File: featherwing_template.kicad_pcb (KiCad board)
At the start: 2 copper layers, 50.8 x 22.9 mm, 3 parts

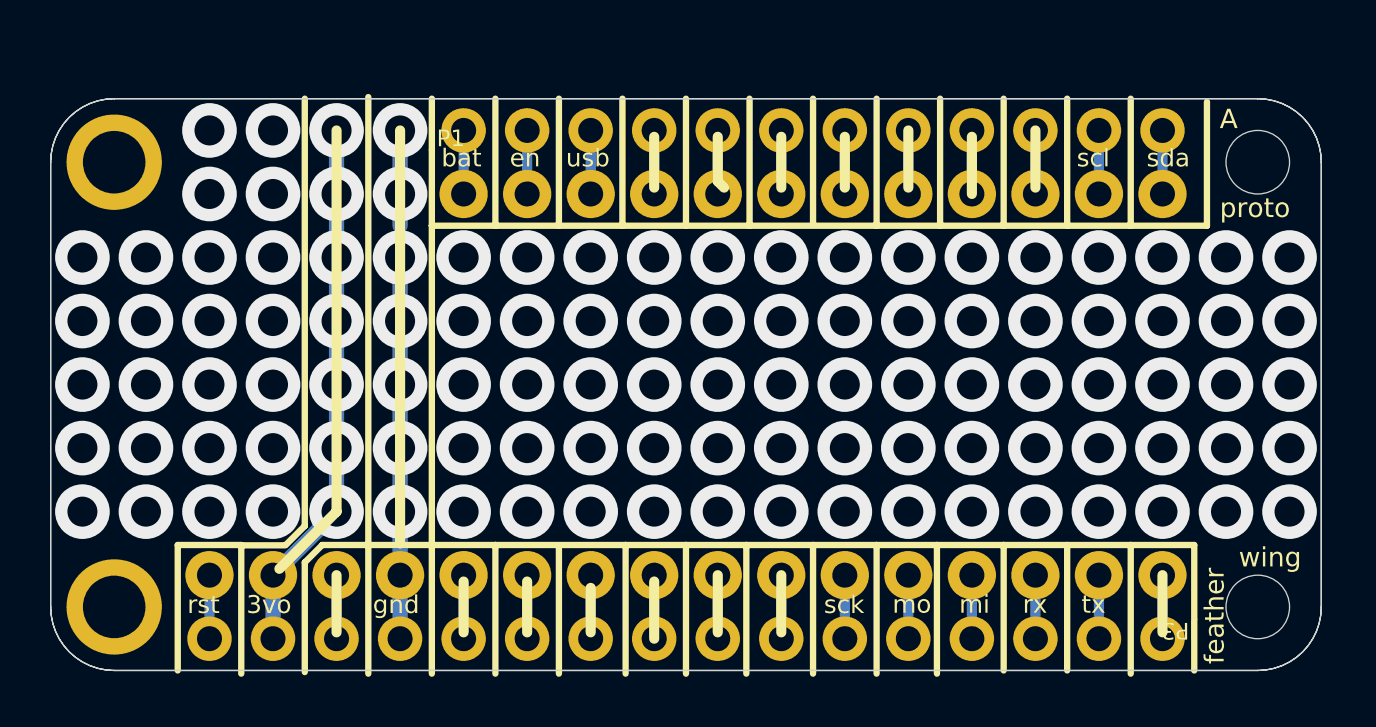
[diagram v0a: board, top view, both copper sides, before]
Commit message: Remove the silkscreen
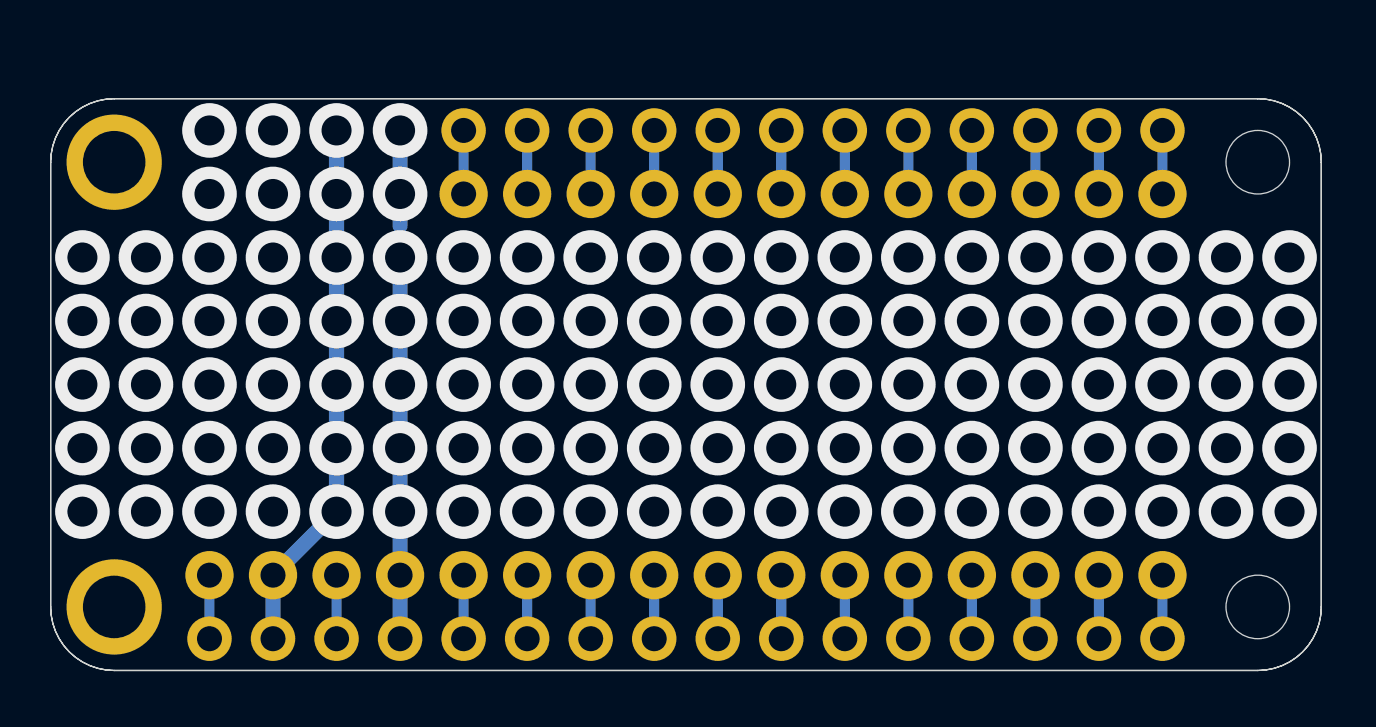
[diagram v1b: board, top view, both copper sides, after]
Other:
- board text removed: "3vo"
- board text removed: "A"
- board text removed: "bat"
- board text removed: "en"
- board text removed: "feather"
- board text removed: "gnd"
- board text removed: "mi"
- board text removed: "mo"
- board text removed: "proto"
- board text removed: "rst"
- board text removed: "rx"
- board text removed: "sck"
- board text removed: "scl"
- board text removed: "sda"
- board text removed: "tx"
- board text removed: "usb"
- board text removed: "wing"

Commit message: REmove all traces and holes (except edge ones)
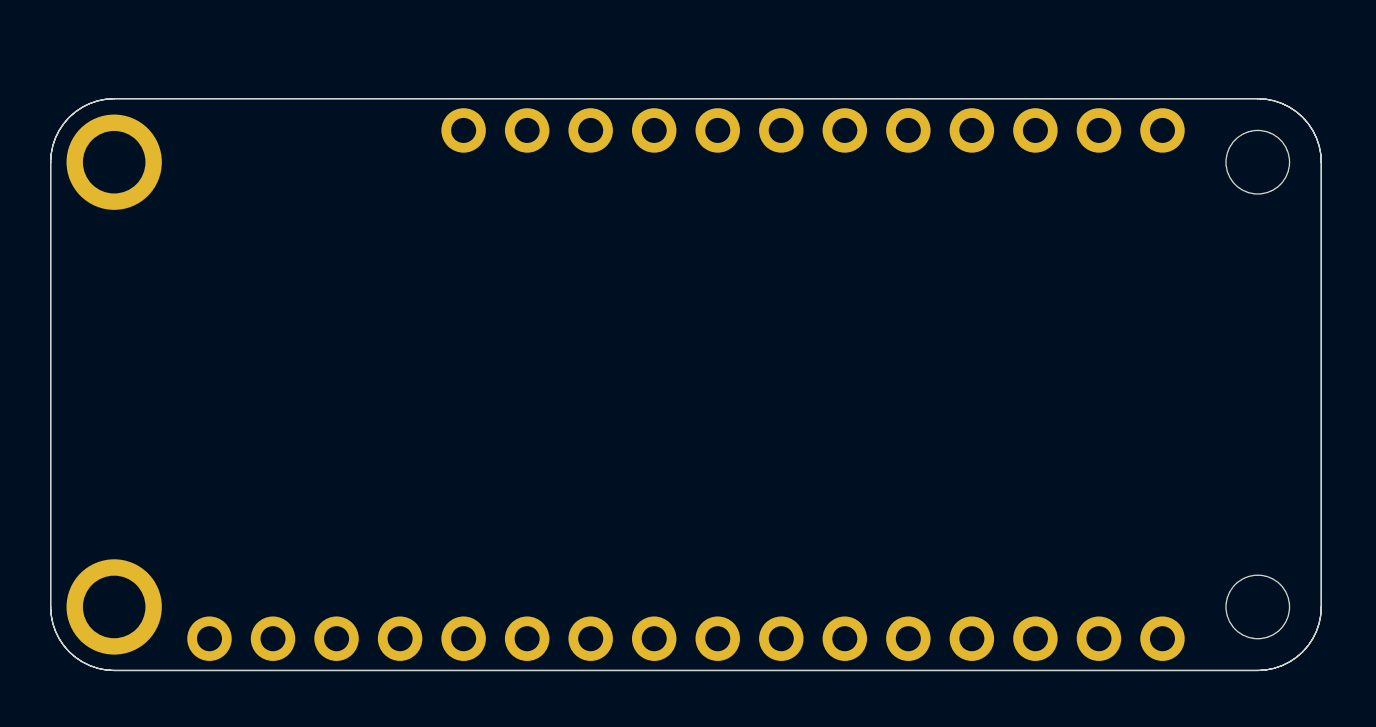
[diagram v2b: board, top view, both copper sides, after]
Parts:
- removed JP1: , featherwing_template:1X12_ROUND_76MIL
- removed JP3: , featherwing_template:1X16_ROUND_76MIL
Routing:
- net 3V: track 21.4 -> 0.00 mm, vias 7 -> 0
- net GND: track 20.3 -> 0.00 mm, vias 7 -> 0
- net VBAT: track 2.54 -> 0.00 mm
- net USB: track 2.54 -> 0.00 mm
- net N$9: track 2.54 -> 0.00 mm
- net N$8: track 2.54 -> 0.00 mm
- net N$7: track 2.54 -> 0.00 mm
- net N$6: track 2.54 -> 0.00 mm
- net N$5: track 2.54 -> 0.00 mm
- net N$4: track 2.54 -> 0.00 mm
- net N$3: track 2.54 -> 0.00 mm
- net N$25: track 2.54 -> 0.00 mm
- net N$24: track 2.54 -> 0.00 mm
- net N$23: track 2.54 -> 0.00 mm
- net N$22: track 2.54 -> 0.00 mm
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
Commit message: Add headers
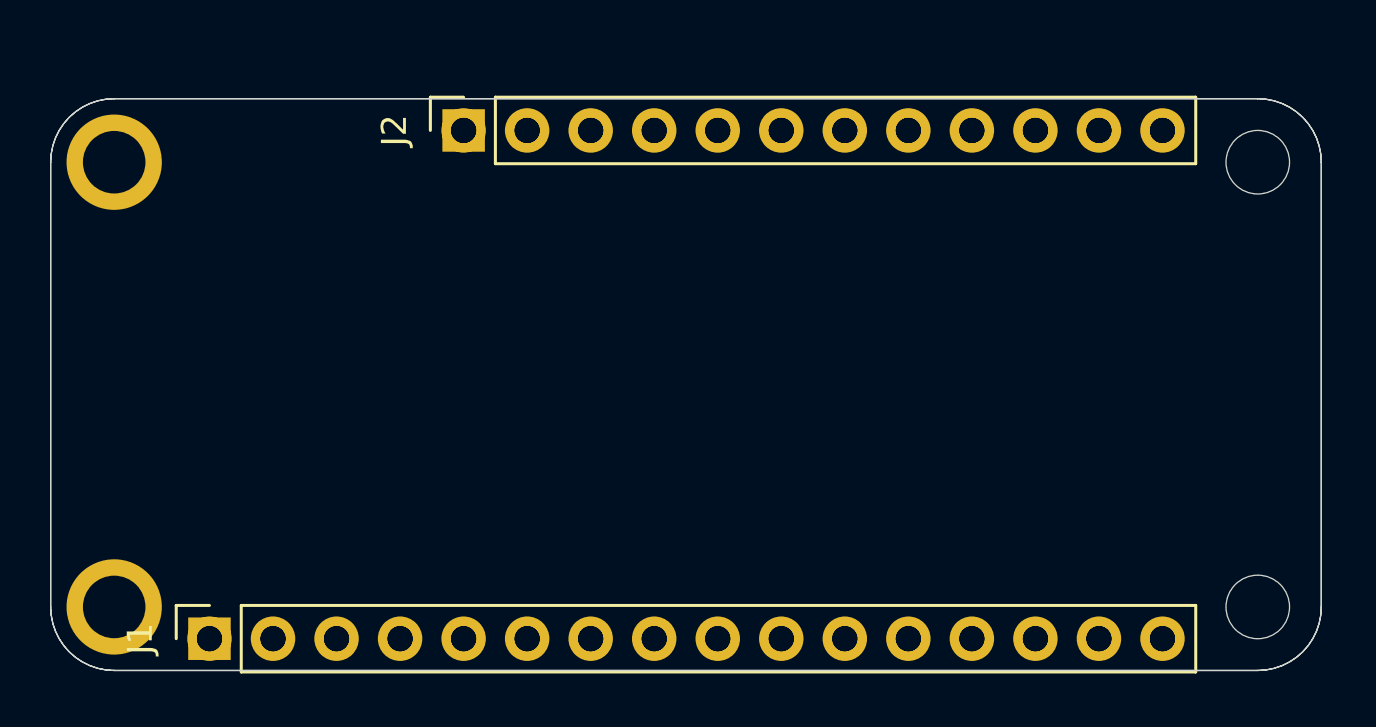
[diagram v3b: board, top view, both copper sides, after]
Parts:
- added J1: Conn_01x16_Socket, Connector_PinSocket_2.54mm:PinSocket_1x16_P2.54mm_Vertical, F.Cu at (129.5, 115.2)
- added J2: Conn_01x12_Socket, Connector_PinSocket_2.54mm:PinSocket_1x12_P2.54mm_Vertical, F.Cu at (139.6, 94.8)

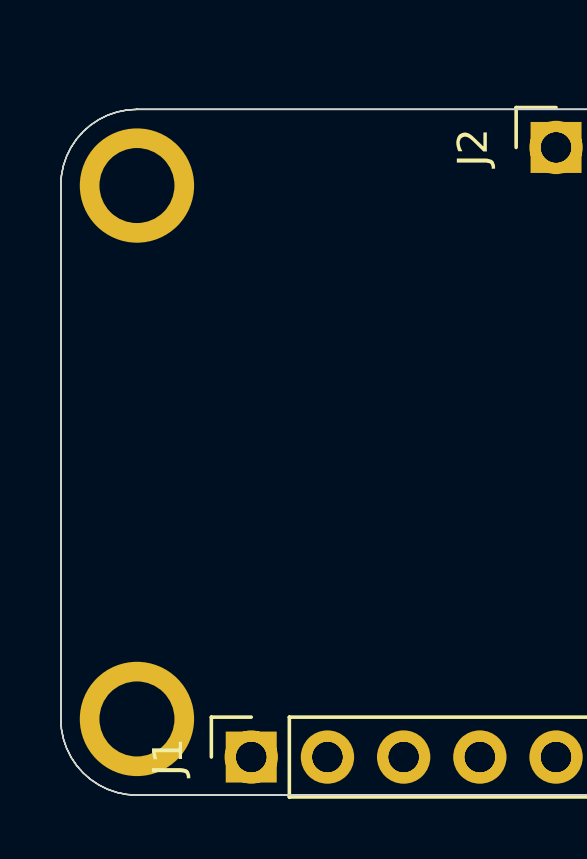
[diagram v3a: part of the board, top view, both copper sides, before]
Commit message: Add plated mounting holes
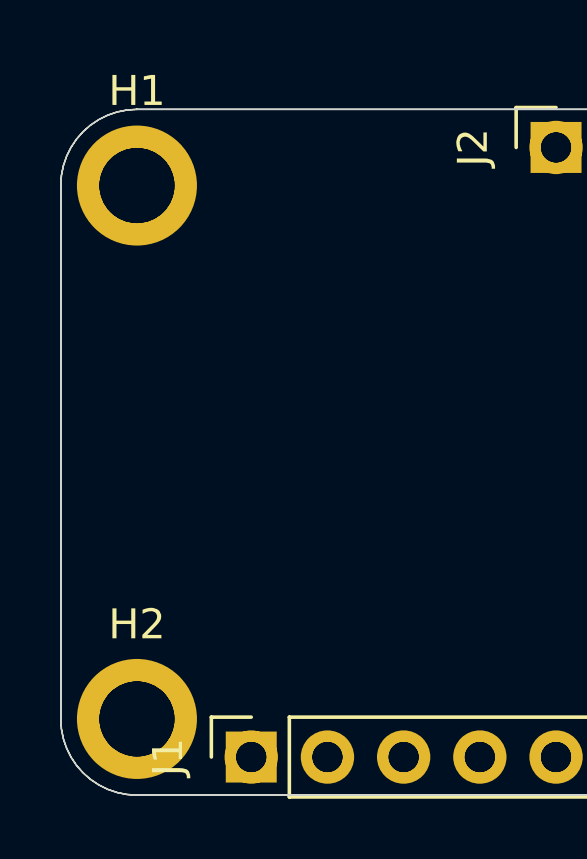
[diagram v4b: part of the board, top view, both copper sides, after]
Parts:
- added H1: MountingHole_Pad, custom:MountingHole_2.5mm, F.Cu at (125.6, 96.1)
- added H2: MountingHole_Pad, custom:MountingHole_2.5mm, F.Cu at (125.6, 113.9)
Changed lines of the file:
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@@
 		)
+	)
+	(footprint "custom:MountingHole_2.5mm"
+		(layer "F.Cu")
+		(at 125.6411 96.1136)
+		(descr "Mounting Hole 2.2mm, M2, generated by kicad-footprint-generator mountinghole.py")
+		(tags "mountinghole M2")
+		(property "Reference" "H1"
+			(at 0 -3.15 0)
+			(layer "F.SilkS")
+			(effects
+				(font
+					(size 1 1)
+					(thickness 0.15)
+				)
+			)
+		)
+		(property "Value" "MountingHole_Pad"
+			(at 0 3.15 0)
+			(layer "F.Fab")
+			(effects
+				(font
+					(size 1 1)
+					(thickness 0.15)
+				)
+			)
+		)
+		(property "Datasheet" "~"
+			(at 0 0 0)
+			(layer "F.Fab")
+			(hide yes)
+			(effects
+				(font
+					(size 1.27 1.27)
+					(thickness 0.15)
+				)
+			)
+		)
+		(property "Description" "Mounting Hole with connection"
+			(at 0 0 0)
+			(layer "F.Fab")
+			(hide yes)
+			(effects
+				(font
+					(size 1.27 1.27)
+					(thickness 0.15)
+				)
+			)
+		)
+		(property ki_fp_filters "MountingHole*Pad*")
+		(sheetname "/")
+		(sheetfile "featherwing_template.kicad_sch")
+		(attr exclude_from_pos_files exclude_from_bom)
+		(fp_circle
+			(center 0 0)
+			(end 1 0)
+			(stroke
+				(width 0.15)
+				(type solid)
+			)
+			(fill no)
+			(layer "Cmts.User")
+		)
+		(fp_circle
+			(center 0 0)
+			(end 1 0)
+			(stroke
+				(width 0.05)
+				(type solid)
+			)
+			(fill no)
+			(layer "F.CrtYd")
+		)
+		(fp_text user "${REFERENCE}"
+			(at 0 0 0)
+			(layer "F.Fab")
+			(effects
+				(font
+					(size 1 1)
+					(thickness 0.15)
+				)
+			)
+		)
+		(pad "1" thru_hole circle
+			(at 0 0)
+			(size 4 4)
+			(drill 2.5)
+			(layers "*.Cu" "*.Mask")
+			(remove_unused_layers no)
+			(net 13 "GND")
+			(pinfunction "1")
+			(pintype "input")
+			(zone_connect 2)
+		)
+		(embedded_fonts no)
 	)
 	(footprint "Connector_PinSocket_2.54mm:PinSocket_1x12_P2.54mm_Vertical"
@@
 		)
 	)
+	(footprint "custom:MountingHole_2.5mm"
+		(layer "F.Cu")
+		(at 125.6411 113.8936)
+		(descr "Mounting Hole 2.2mm, M2, generated by kicad-footprint-generator mountinghole.py")
+		(tags "mountinghole M2")
+		(property "Reference" "H2"
+			(at 0 -3.15 0)
+			(layer "F.SilkS")
+			(effects
+				(font
+					(size 1 1)
+					(thickness 0.15)
+				)
+			)
+		)
+		(property "Value" "MountingHole_Pad"
+			(at 0 3.15 0)
+			(layer "F.Fab")
+			(effects
+				(font
+					(size 1 1)
+					(thickness 0.15)
+				)
+			)
+		)
+		(property "Datasheet" "~"
+			(at 0 0 0)
+			(layer "F.Fab")
+			(hide yes)
+			(effects
+				(font
+					(size 1.27 1.27)
+					(thickness 0.15)
+				)
+			)
+		)
+		(property "Description" "Mounting Hole with connection"
+			(at 0 0 0)
+			(layer "F.Fab")
+			(hide yes)
+			(effects
+				(font
+					(size 1.27 1.27)
+					(thickness 0.15)
+				)
+			)
+		)
+		(property ki_fp_filters "MountingHole*Pad*")
+		(sheetname "/")
+		(sheetfile "featherwing_template.kicad_sch")
+		(attr exclude_from_pos_files exclude_from_bom)
+		(fp_circle
+			(center 0 0)
+			(end 1 0)
+			(stroke
+				(width 0.15)
+				(type solid)
+			)
+			(fill no)
+			(layer "Cmts.User")
+		)
+		(fp_circle
+			(center 0 0)
+			(end 1 0)
+			(stroke
+				(width 0.05)
+				(type solid)
+			)
+			(fill no)
+			(layer "F.CrtYd")
+		)
+		(fp_text user "${REFERENCE}"
+			(at 0 0 0)
+			(layer "F.Fab")
+			(effects
+				(font
+					(size 1 1)
+					(thickness 0.15)
+				)
+			)
+		)
+		(pad "1" thru_hole circle
+			(at 0 0)
+			(size 4 4)
+			(drill 2.5)
+			(layers "*.Cu" "*.Mask")
+			(remove_unused_layers no)
+			(net 13 "GND")
+			(pinfunction "1")
+			(pintype "input")
+			(zone_connect 2)
+		)
+		(embedded_fonts no)
+	)
 	(gr_arc

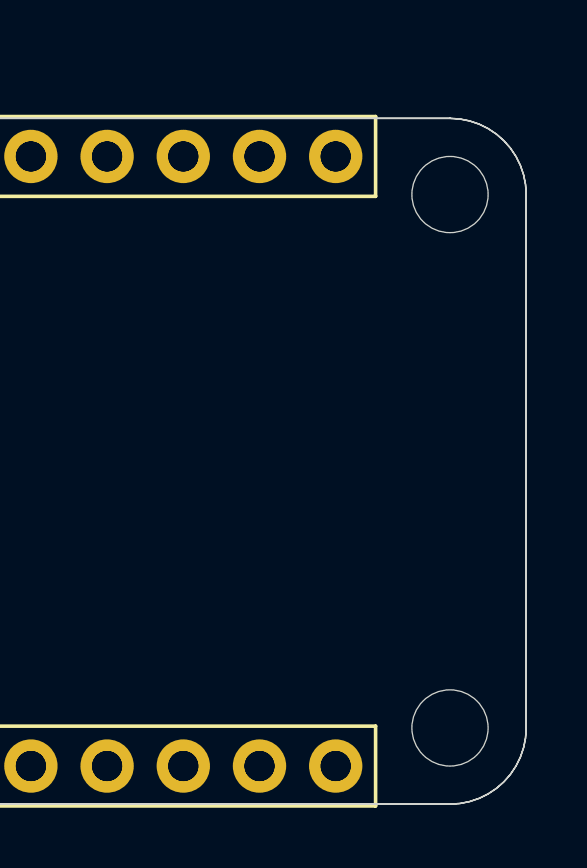
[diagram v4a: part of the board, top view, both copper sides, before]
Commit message: Add nonplated mounting holes
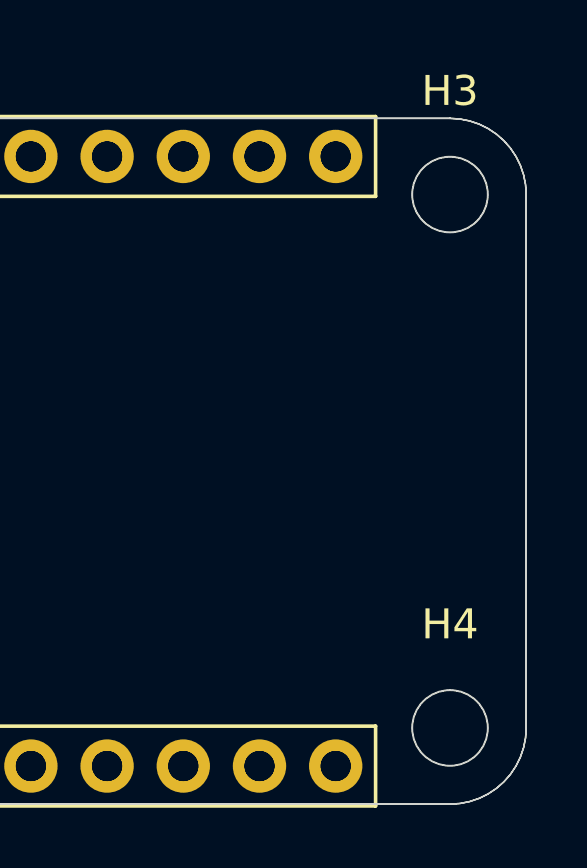
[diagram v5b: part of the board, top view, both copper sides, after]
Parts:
- added H3: MountingHole, MountingHole:MountingHole_2.5mm, F.Cu at (171.4, 96.1)
- added H4: MountingHole, MountingHole:MountingHole_2.5mm, F.Cu at (171.4, 113.9)
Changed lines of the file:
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@@
+		(embedded_fonts no)
+	)
+	(footprint "MountingHole:MountingHole_2.5mm"
+		(layer "F.Cu")
+		(at 171.3611 113.8936)
+		(descr "Mounting Hole 2.5mm, no annular, generated by kicad-footprint-generator mountinghole.py")
+		(tags "mountinghole")
+		(property "Reference" "H4"
+			(at 0 -3.45 0)
+			(layer "F.SilkS")
+			(effects
+				(font
+					(size 1 1)
+					(thickness 0.15)
+				)
+			)
+		)
+		(property "Value" "MountingHole"
+			(at 0 3.45 0)
+			(layer "F.Fab")
+			(effects
+				(font
+					(size 1 1)
+					(thickness 0.15)
+				)
+			)
+		)
+		(property "Datasheet" "~"
+			(at 0 0 0)
+			(layer "F.Fab")
+			(hide yes)
+			(effects
+				(font
+					(size 1.27 1.27)
+					(thickness 0.15)
+				)
+			)
+		)
+		(property "Description" "Mounting Hole without connection"
+			(at 0 0 0)
+			(layer "F.Fab")
+			(hide yes)
+			(effects
+				(font
+					(size 1.27 1.27)
+					(thickness 0.15)
+				)
+			)
+		)
+		(property ki_fp_filters "MountingHole*")
+		(sheetname "/")
+		(sheetfile "featherwing_template.kicad_sch")
+		(attr exclude_from_pos_files exclude_from_bom)
+		(fp_circle
+			(center 0 0)
+			(end 2.5 0)
+			(stroke
+				(width 0.15)
+				(type solid)
+			)
+			(fill no)
+			(layer "Cmts.User")
+		)
+		(fp_circle
+			(center 0 0)
+			(end 2.75 0)
+			(stroke
+				(width 0.05)
+				(type solid)
+			)
+			(fill no)
+			(layer "F.CrtYd")
+		)
+		(fp_text user "${REFERENCE}"
+			(at 0 0 0)
+			(layer "F.Fab")
+			(effects
+				(font
+					(size 1 1)
+					(thickness 0.15)
+				)
+			)
+		)
+		(pad "" np_thru_hole circle
+			(at 0 0)
+			(size 2.5 2.5)
+			(drill 2.5)
+			(layers "*.Cu" "*.Mask")
+		)
+		(embedded_fonts no)
+	)
+	(footprint "MountingHole:MountingHole_2.5mm"
+		(layer "F.Cu")
+		(at 171.3611 96.1136)
+		(descr "Mounting Hole 2.5mm, no annular, generated by kicad-footprint-generator mountinghole.py")
+		(tags "mountinghole")
+		(property "Reference" "H3"
+			(at 0 -3.45 0)
+			(layer "F.SilkS")
+			(effects
+				(font
+					(size 1 1)
+					(thickness 0.15)
+				)
+			)
+		)
+		(property "Value" "MountingHole"
+			(at 0 3.45 0)
+			(layer "F.Fab")
+			(effects
+				(font
+					(size 1 1)
+					(thickness 0.15)
+				)
+			)
+		)
+		(property "Datasheet" "~"
+			(at 0 0 0)
+			(layer "F.Fab")
+			(hide yes)
+			(effects
+				(font
+					(size 1.27 1.27)
+					(thickness 0.15)
+				)
+			)
+		)
+		(property "Description" "Mounting Hole without connection"
+			(at 0 0 0)
+			(layer "F.Fab")
+			(hide yes)
+			(effects
+				(font
+					(size 1.27 1.27)
+					(thickness 0.15)
+				)
+			)
+		)
+		(property ki_fp_filters "MountingHole*")
+		(sheetname "/")
+		(sheetfile "featherwing_template.kicad_sch")
+		(attr exclude_from_pos_files exclude_from_bom)
+		(fp_circle
+			(center 0 0)
+			(end 2.5 0)
+			(stroke
+				(width 0.15)
+				(type solid)
+			)
+			(fill no)
+			(layer "Cmts.User")
+		)
+		(fp_circle
+			(center 0 0)
+			(end 2.75 0)
+			(stroke
+				(width 0.05)
+				(type solid)
+			)
+			(fill no)
+			(layer "F.CrtYd")
+		)
+		(fp_text user "${REFERENCE}"
+			(at 0 0 0)
+			(layer "F.Fab")
+			(effects
+				(font
+					(size 1 1)
+					(thickness 0.15)
+				)
+			)
+		)
+		(pad "" np_thru_hole circle
+			(at 0 0)
+			(size 2.5 2.5)
+			(drill 2.5)
+			(layers "*.Cu" "*.Mask")
+		)
 		(embedded_fonts no)
 	)
